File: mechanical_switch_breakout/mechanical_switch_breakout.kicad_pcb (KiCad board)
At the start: 2 copper layers, 68 x 18 mm, 4 parts, among them J1 Conn_01x04_Pin, SW1 SW_SPST, SW2 SW_SPST, SW3 SW_SPST

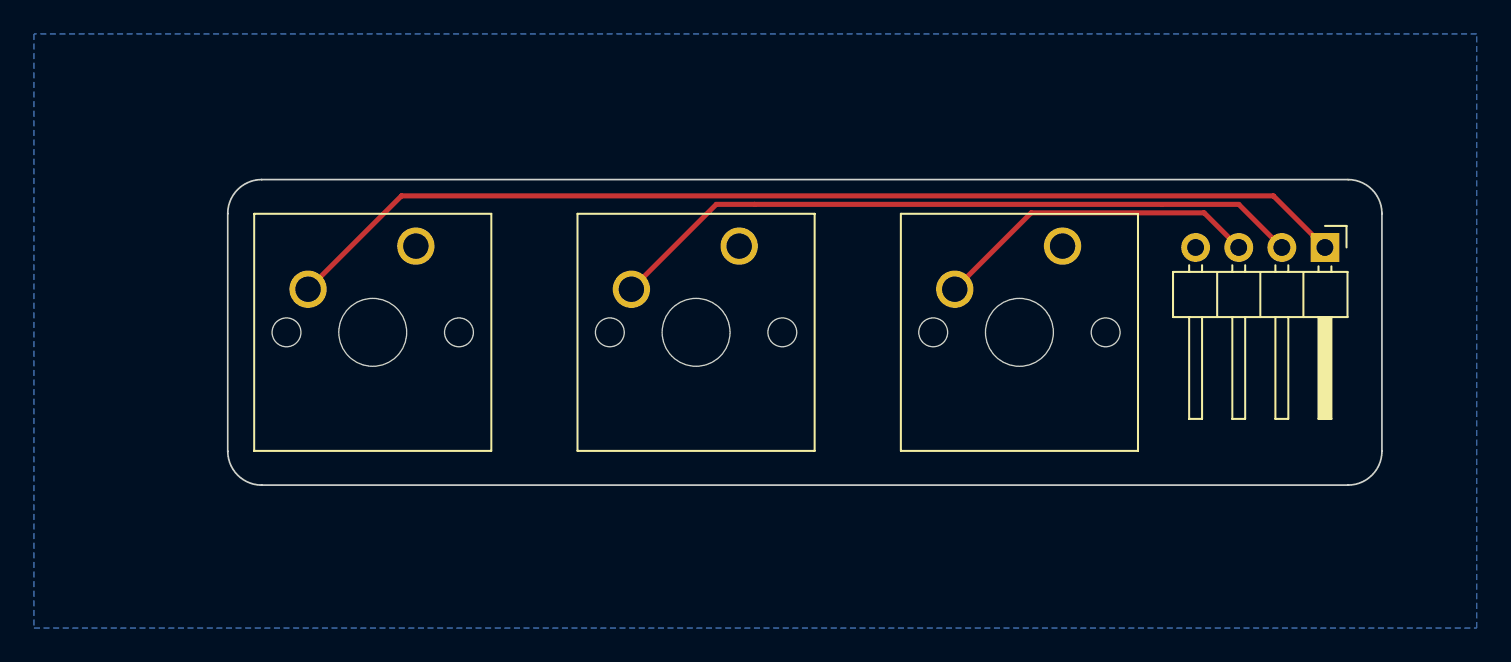
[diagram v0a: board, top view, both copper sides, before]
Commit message: Added casing cad files
Designed a case in Onshape, made minor revisions to breakout boards.
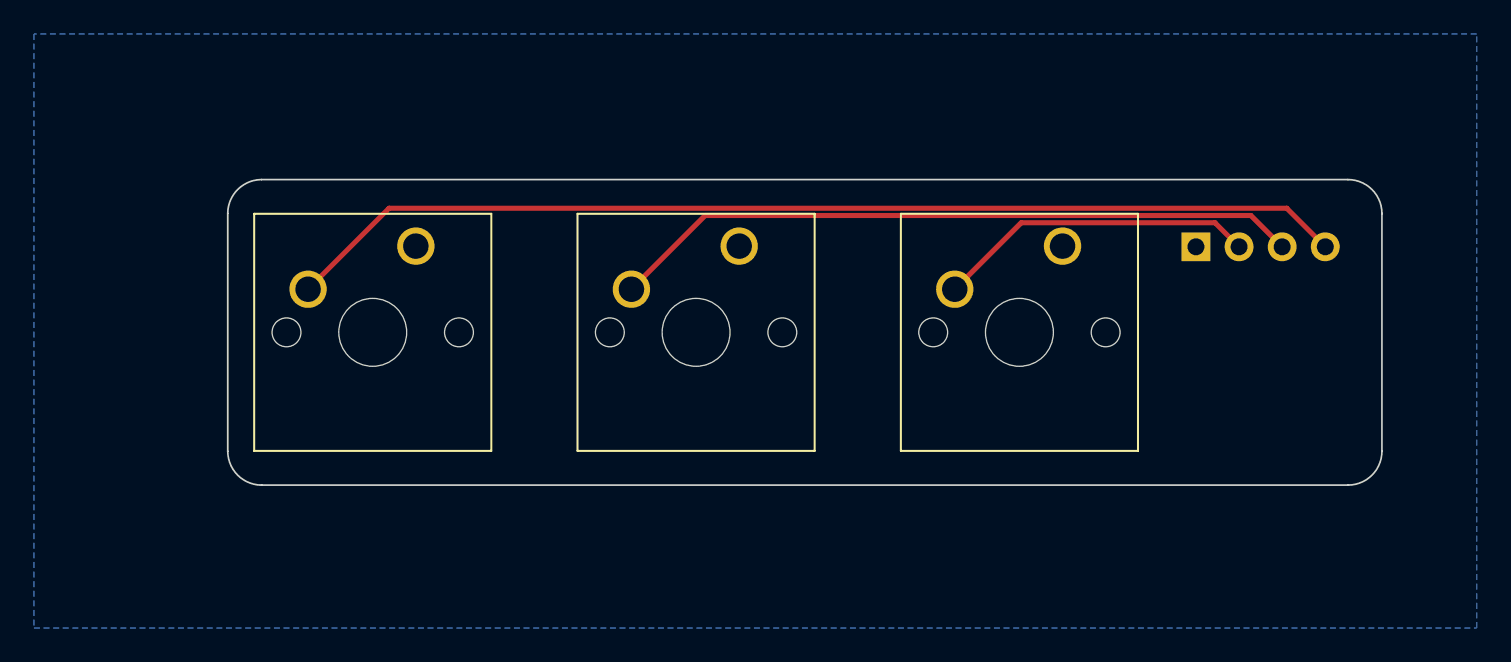
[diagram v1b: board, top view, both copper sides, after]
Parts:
- J1: moved to B.Cu
- moved J1 7.60 mm to (126.0, 58.5)
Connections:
- J1 pad 1: /SW_1 -> /COMMON
- J1 pad 2: /SW_2 -> /SW_3
- J1 pad 3: /SW_3 -> /SW_2
- J1 pad 4: /COMMON -> /SW_1
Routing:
- net /SW_1: track 63.4 -> 62.8 mm
- net /SW_2: track 41.4 -> 40.9 mm
